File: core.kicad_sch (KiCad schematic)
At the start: 1 part, among them U2 RP2040TR7

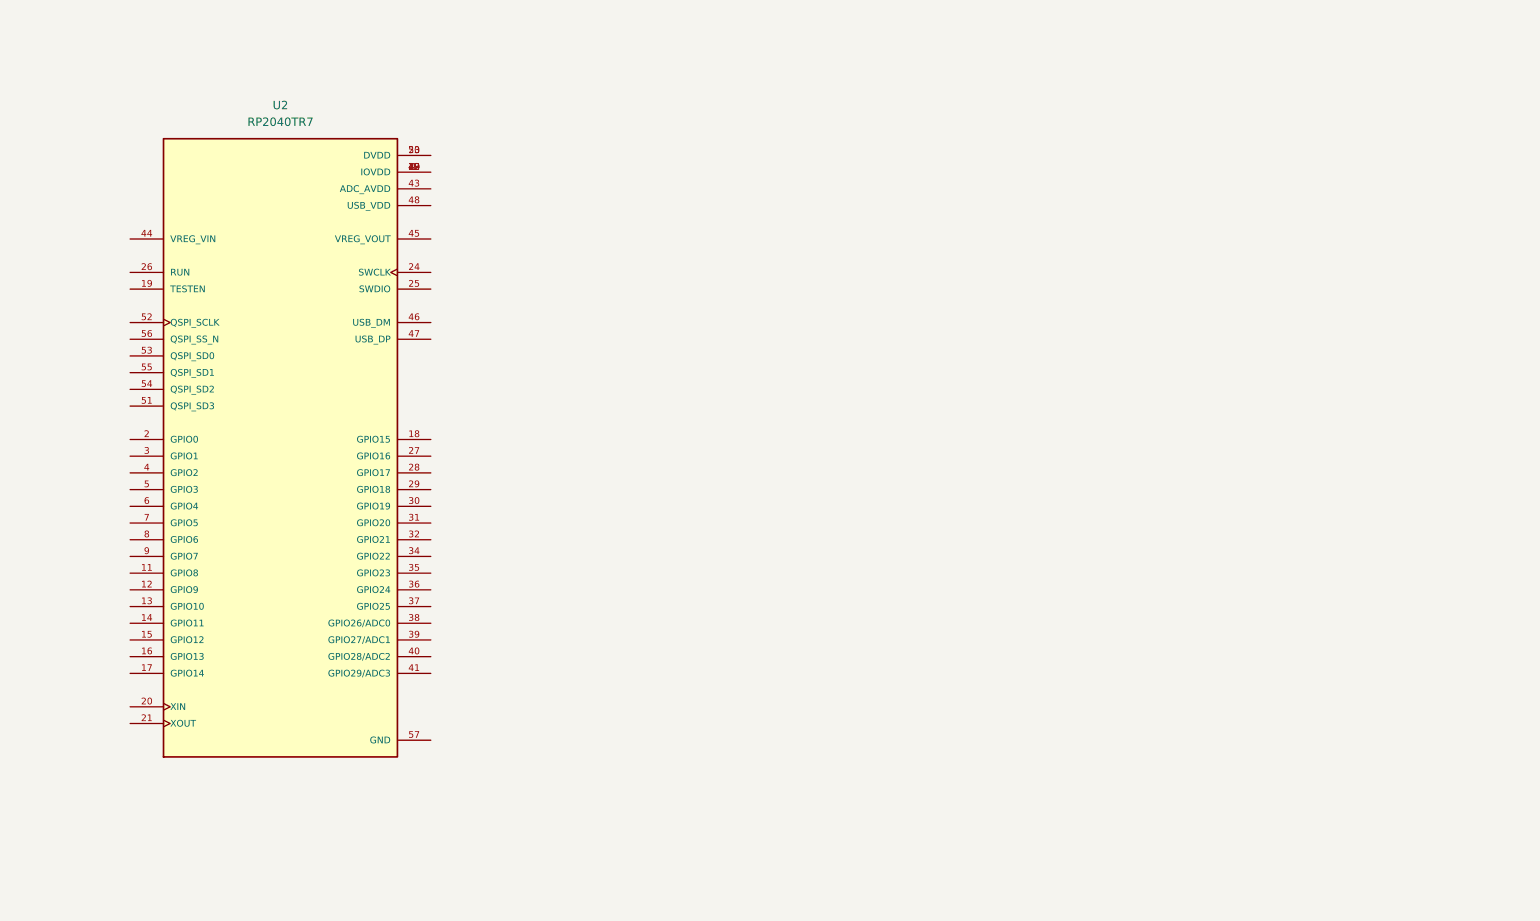
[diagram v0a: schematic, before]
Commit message: Add partial RF and Memory wiring and placement
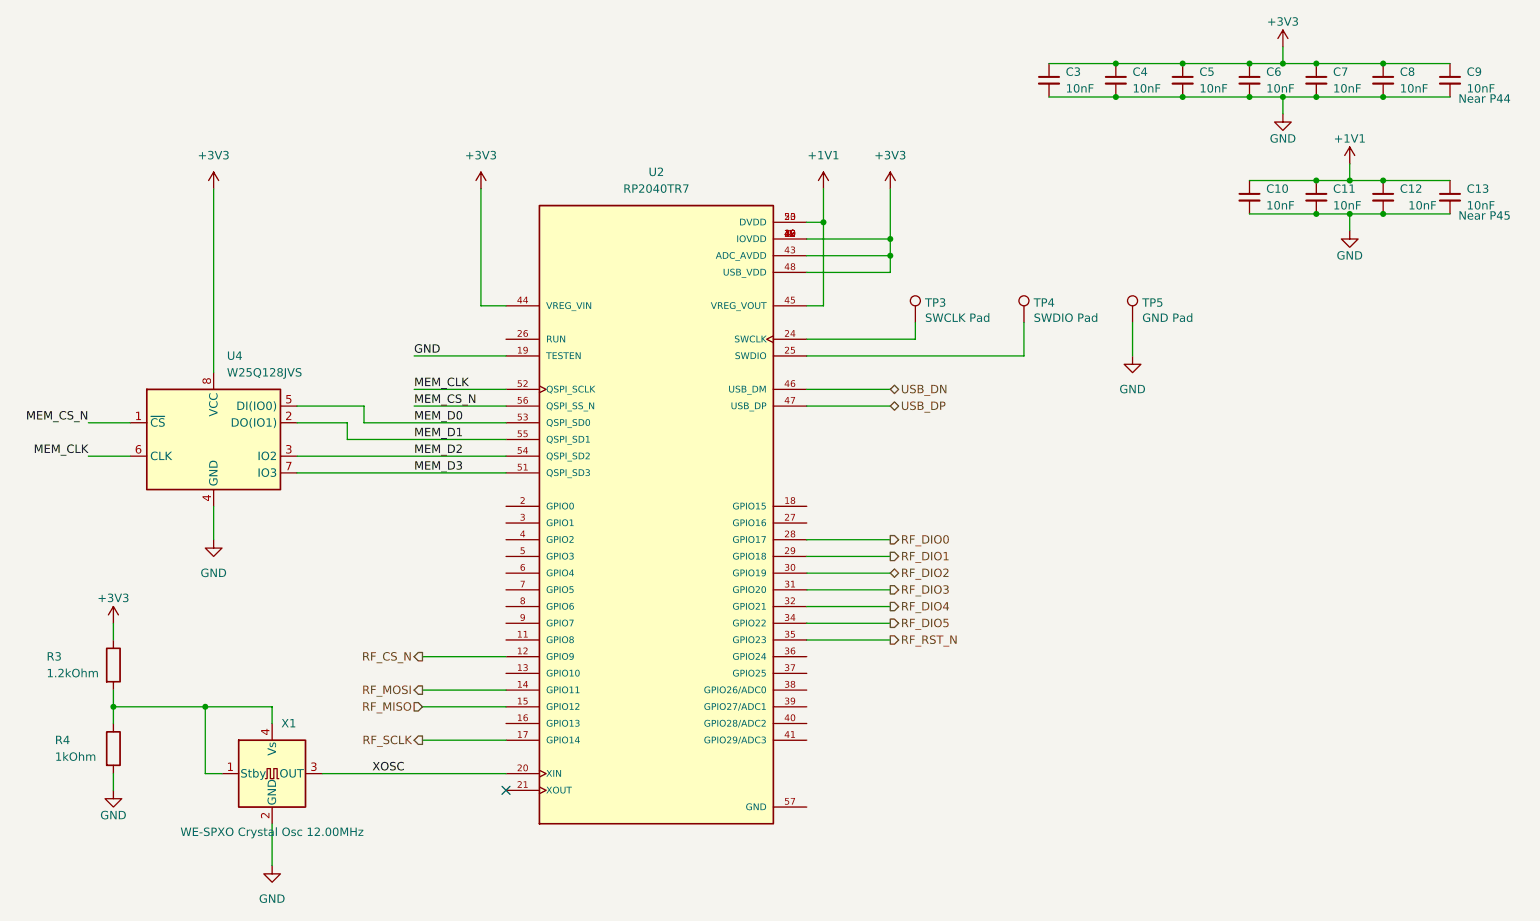
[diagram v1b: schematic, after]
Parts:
- added C10, C11, C12, C13, C3, C4, C5, C6, C7, C8, C9: 10nF, Capacitor_SMD:C_0402_1005Metric, symbol Device:C_Small
- added R3: 1.2kOhm, Resistor_SMD:R_0402_1005Metric, symbol Device:R
- added R4: 1kOhm, Resistor_SMD:R_0402_1005Metric, symbol Device:R
- added TP3: SWCLK Pad, TestPoint:TestPoint_Pad_1.5x1.5mm, symbol Connector:TestPoint
- added TP4: SWDIO Pad, TestPoint:TestPoint_Pad_1.5x1.5mm, symbol Connector:TestPoint
- added TP5: GND Pad, TestPoint:TestPoint_Pad_1.5x1.5mm, symbol Connector:TestPoint
- added U4: W25Q128JVS, Package_SON:WSON-8-1EP_6x5mm_P1.27mm_EP3.4x4mm, symbol Memory_Flash:W25Q128JVS
- added X1: WE-SPXO Crystal Osc 12.00MHz, KKicadLib:Oscillator_SMD_4pin_2.5x2.0mm, symbol KKicadLib:WE-SPXO Crystal Osc 12.00MHz
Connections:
- net +3V3: now reaches U2.1 (IOVDD), U2.10 (IOVDD), U2.22 (IOVDD), U2.33 (IOVDD), U2.42 (IOVDD), U2.49 (IOVDD)
- net +3V3: now also U2.43 (ADC_AVDD), U2.44 (VREG_VIN), U2.48 (USB_VDD), C3.1, C4.1, C5.1, C6.1, C7.1, C8.1, C9.1, R3.1, U4.8 (VCC)
- net RF_CS_N: now reaches U2.12 (GPIO9)
- net RF_MOSI: now reaches U2.14 (GPIO11)
- net RF_MISO: now reaches U2.15 (GPIO12)
- net RF_SCLK: now reaches U2.17 (GPIO14)
- net GND: now reaches U2.19 (TESTEN)
- net GND: now also C10.2, C11.2, C12.2, C13.2, C3.2, C4.2, C5.2, C6.2, C7.2, C8.2, C9.2, R4.2, TP5.1, U4.4 (GND), X1.2 (GND)
- net XOSC: now reaches U2.20 (XIN)
- net XOSC: now also X1.3 (OUT)
- net +1V1: now reaches U2.23 (DVDD), U2.50 (DVDD)
- net +1V1: now also U2.45 (VREG_VOUT), C10.1, C11.1, C12.1, C13.1
- net at U2.24 (SWCLK): now also TP3.1
- net at U2.25 (SWDIO): now also TP4.1
- net RF_DIO0: now reaches U2.28 (GPIO17)
- net RF_DIO1: now reaches U2.29 (GPIO18)
- net RF_DIO2: now reaches U2.30 (GPIO19)
- net RF_DIO3: now reaches U2.31 (GPIO20)
- net RF_DIO4: now reaches U2.32 (GPIO21)
- net RF_DIO5: now reaches U2.34 (GPIO22)
- net RF_RST_N: now reaches U2.35 (GPIO23)
- net USB_DN: now reaches U2.46 (USB_DM)
- net USB_DP: now reaches U2.47 (USB_DP)
- net MEM_D3: now reaches U2.51 (QSPI_SD3)
- net MEM_D3: now also U4.7 (IO3)
- net MEM_CLK: now reaches U2.52 (QSPI_SCLK)
- net MEM_CLK: now also U4.6 (CLK)
- net MEM_D0: now reaches U2.53 (QSPI_SD0)
- net MEM_D0: now also U4.5 (DI(IO0))
- net MEM_D2: now reaches U2.54 (QSPI_SD2)
- net MEM_D2: now also U4.3 (IO2)
- net MEM_D1: now reaches U2.55 (QSPI_SD1)
- net MEM_D1: now also U4.2 (DO(IO1))
- net MEM_CS_N: now reaches U2.56 (QSPI_SS_N)
- net MEM_CS_N: now also U4.1 (~{CS})
- new net: R3.2, R4.1, X1.1 (Stby), X1.4 (Vs)
- no-connect marks 0 -> 1
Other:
- note added: "Near P44"
- note added: "Near P45"
- title: (none) -> LoRa Expansion Card for Frame.Work Laptop
- moved on the sheet: U2
